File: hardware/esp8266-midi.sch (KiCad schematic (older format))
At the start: 20 parts, among them J1 MIDI in, J2 MIDI out, J3 TTL-232R-3V3 connector, J4 Bat+, J5 Bat-, U1 ESP-12E, U2 6N138, U3 LD1117S50TR_SOT223

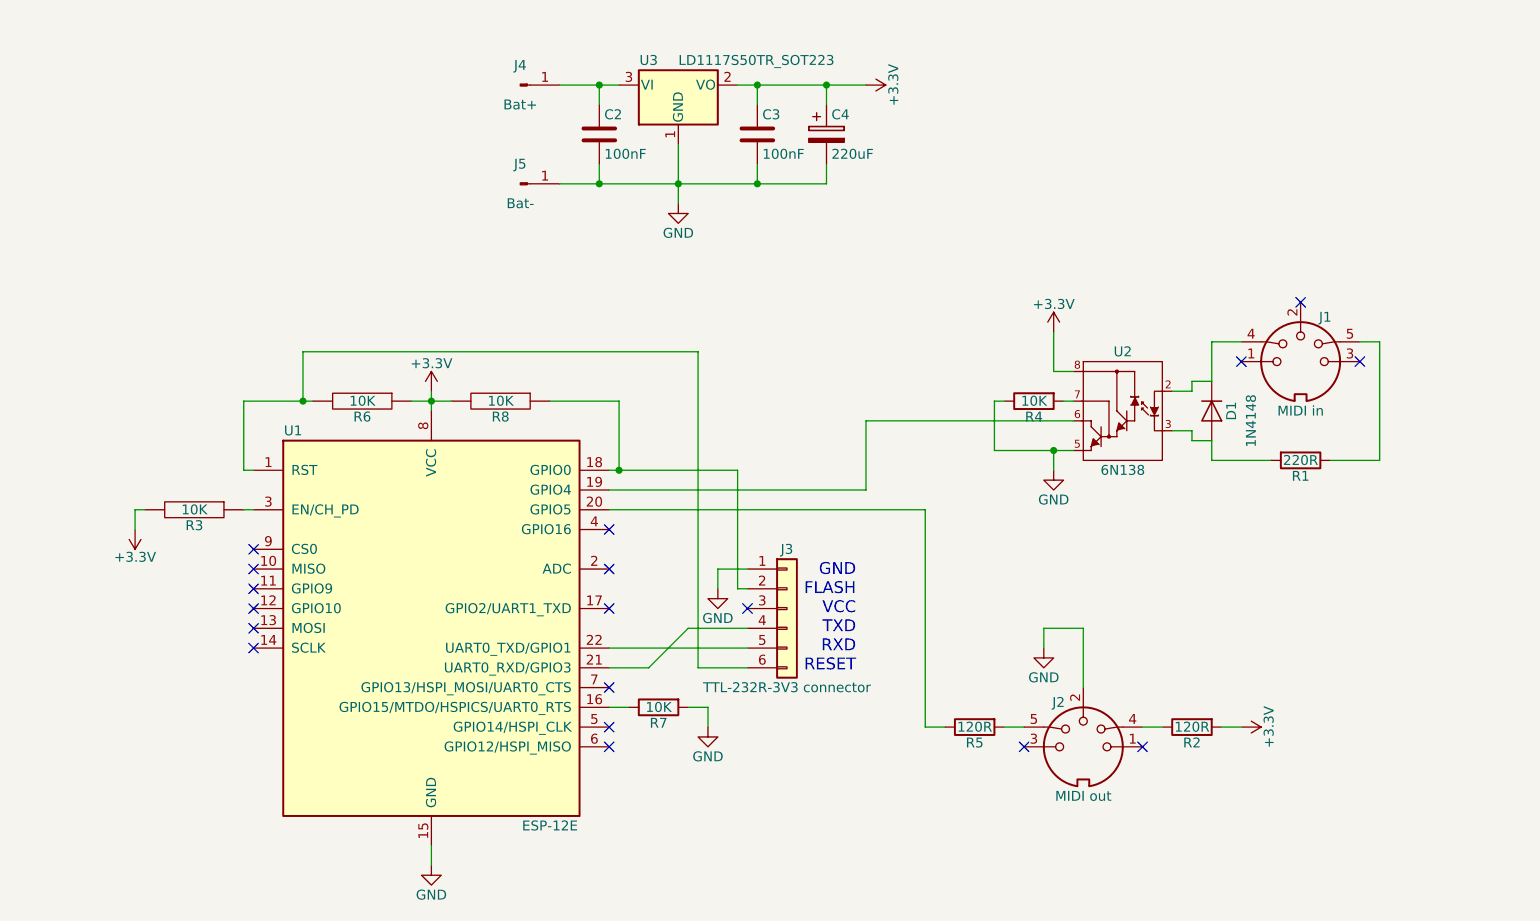
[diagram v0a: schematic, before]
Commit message: Schematic changes: midi through, midi via hardware serial, debug serial out
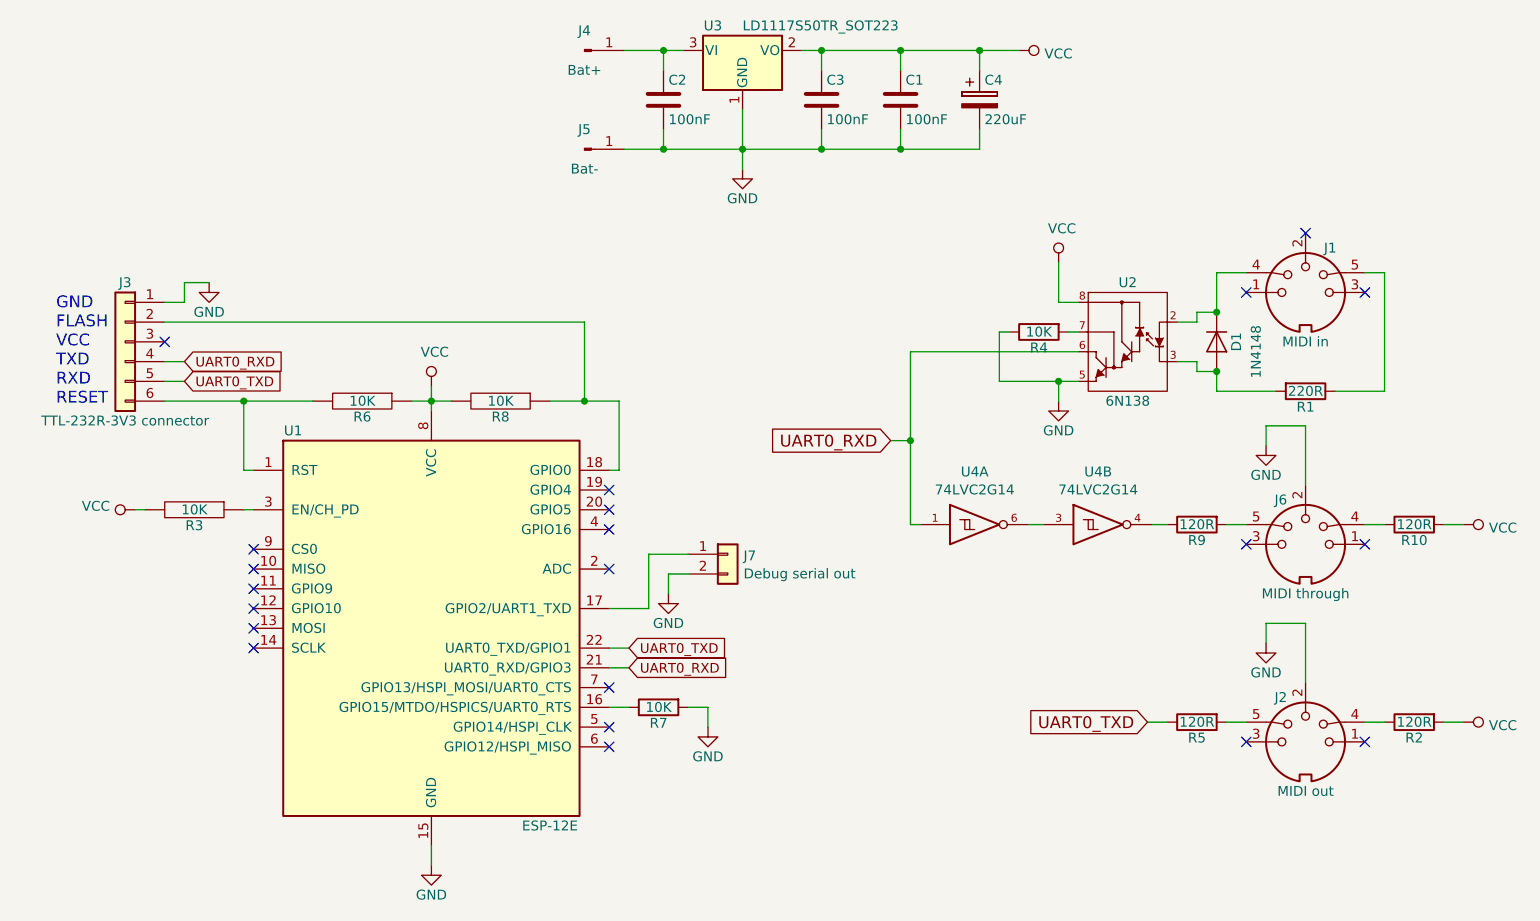
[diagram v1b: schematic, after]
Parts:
- added C1: 100nF, Capacitors_SMD:C_0805_HandSoldering, symbol esp8266-midi-rescue:C-RESCUE-esp8266-midi
- added J6: MIDI through, Connectors:SDS-50J, symbol Connector1:DIN-5_180degree
- added J7: Debug serial out, Pin_Headers:Pin_Header_Straight_1x02_Pitch2.54mm, symbol Connector1:Conn_01x02
- added R10, R9: 120R, Resistors_SMD:R_0805_HandSoldering, symbol esp8266-midi-rescue:R-RESCUE-esp8266-midi
- added U4: 74LVC2G14, TO_SOT_Packages_SMD:SOT-23-6_Handsoldering, symbol 74xGxx:74LVC2G14
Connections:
- net GND: now also C1.2, J6.2, J7.2 (Pin_2), U4.2 (GND), U4.2 (GND)
- net at U1.20 (GPIO5): no longer R5.1
- net at U1.19 (GPIO4): no longer U2.6 (Vo)
- net UART0_RXD: now reaches J3.4 (Pin_4), U1.21 (UART0_RXD/GPIO3)
- net UART0_RXD: now also U2.6 (Vo), U4.1
- net UART0_TXD: now reaches J3.5 (Pin_5), U1.22 (UART0_TXD/GPIO1)
- net UART0_TXD: now also R5.1
- net at U1.17 (GPIO2/UART1_TXD): now also J7.1 (Pin_1)
- net +3V3 renamed VCC
- net VCC: now also C1.1, R10.2, U4.5 (VCC), U4.5 (VCC)
- new net: U4.3, U4.6
- new net: R9.1, U4.4
- new net: J6.4, R10.1
- new net: J6.5, R9.2
- no-connect marks 18 -> 21
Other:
- moved on the sheet: C2, C3, C4, D1, J1, J2, J3, J4, J5, R1, R2, R4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
